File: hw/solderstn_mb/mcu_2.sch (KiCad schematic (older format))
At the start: 21 parts, among them U401 STM32F429VITx, U402 REF6125IDGK, U403 TLV9052SIDGS

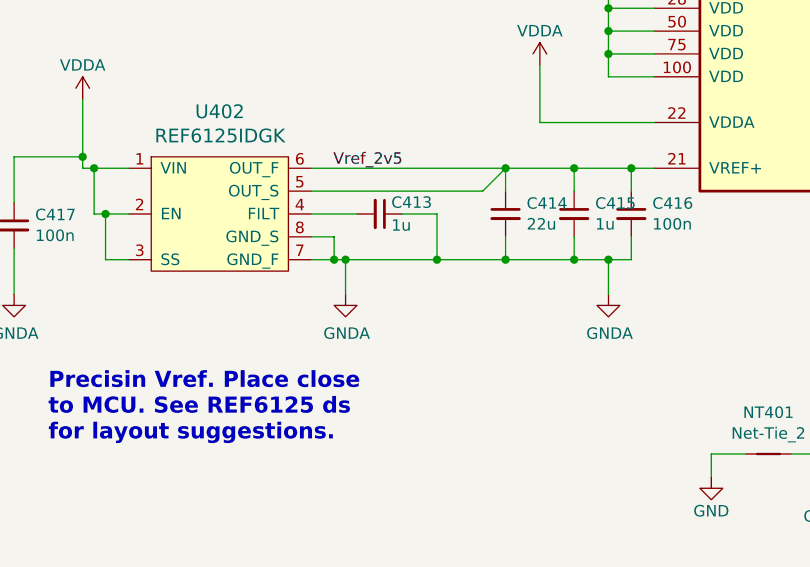
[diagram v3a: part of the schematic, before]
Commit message: Corrected several ERC issues. Re-annotated & assigned all footprints except 32k xtal (will prob. replace with RTC module anyway)
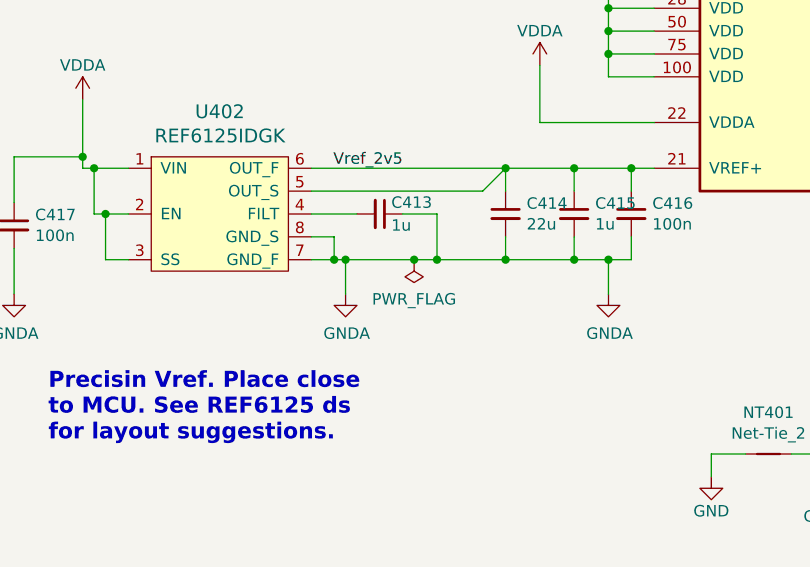
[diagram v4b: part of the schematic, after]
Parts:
- C401, C409, C410, C411, C412, C413, C414, C415, C416, C417: footprint (none) -> Capacitor_SMD:C_0603_1608Metric
- C402, C403, C404, C405, C406, C407, C408: footprint (none) -> Capacitor_SMD:C_0402_1005Metric
- NT401: footprint (none) -> NetTie:NetTie-2_SMD_Pad2.0mm
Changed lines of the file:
@@
 F 0 "C414" H 4442 3546 50  0000 L CNN
 F 1 "22u" H 4442 3455 50  0000 L CNN
-F 2 "" H 4350 3500 50  0001 C CNN
+F 2 "Capacitor_SMD:C_0603_1608Metric" H 4350 3500 50  0001 C CNN
 F 3 "~" H 4350 3500 50  0001 C CNN
 	1    4350 3500
@@
 F 0 "C413" V 3750 3550 50  0000 L CNN
 F 1 "1u" V 3850 3550 50  0000 L CNN
-F 2 "" H 3800 3500 50  0001 C CNN
+F 2 "Capacitor_SMD:C_0603_1608Metric" H 3800 3500 50  0001 C CNN
 F 3 "~" H 3800 3500 50  0001 C CNN
 	1    3800 3500
@@
 Connection ~ 4050 3700
 Wire Wire Line
-	4050 3700 3650 3700
+	4050 3700 3950 3700
 Wire Wire Line
 	3700 3500 3500 3500
@@
 F 0 "C417" H 2292 3596 50  0000 L CNN
 F 1 "100n" H 2292 3505 50  0000 L CNN
-F 2 "" H 2200 3550 50  0001 C CNN
+F 2 "Capacitor_SMD:C_0603_1608Metric" H 2200 3550 50  0001 C CNN
 F 3 "~" H 2200 3550 50  0001 C CNN
 	1    2200 3550
@@
 F 0 "C411" H 8242 3296 50  0000 L CNN
 F 1 "100n" H 8242 3205 50  0000 L CNN
-F 2 "" H 8150 3250 50  0001 C CNN
+F 2 "Capacitor_SMD:C_0603_1608Metric" H 8150 3250 50  0001 C CNN
 F 3 "~" H 8150 3250 50  0001 C CNN
 	1    8150 3250
@@
 F 0 "C408" H 10142 2296 50  0000 L CNN
 F 1 "100n" H 10142 2205 50  0000 L CNN
-F 2 "" H 10050 2250 50  0001 C CNN
+F 2 "Capacitor_SMD:C_0402_1005Metric" H 10050 2250 50  0001 C CNN
 F 3 "~" H 10050 2250 50  0001 C CNN
 	1    10050 2250
@@
 F 0 "C407" H 9792 2296 50  0000 L CNN
 F 1 "100n" H 9792 2205 50  0000 L CNN
-F 2 "" H 9700 2250 50  0001 C CNN
+F 2 "Capacitor_SMD:C_0402_1005Metric" H 9700 2250 50  0001 C CNN
 F 3 "~" H 9700 2250 50  0001 C CNN
 	1    9700 2250
@@
 F 0 "C406" H 9442 2296 50  0000 L CNN
 F 1 "100n" H 9442 2205 50  0000 L CNN
-F 2 "" H 9350 2250 50  0001 C CNN
+F 2 "Capacitor_SMD:C_0402_1005Metric" H 9350 2250 50  0001 C CNN
 F 3 "~" H 9350 2250 50  0001 C CNN
 	1    9350 2250
@@
 F 0 "C405" H 9092 2296 50  0000 L CNN
 F 1 "100n" H 9092 2205 50  0000 L CNN
-F 2 "" H 9000 2250 50  0001 C CNN
+F 2 "Capacitor_SMD:C_0402_1005Metric" H 9000 2250 50  0001 C CNN
 F 3 "~" H 9000 2250 50  0001 C CNN
 	1    9000 2250
@@
 F 0 "C404" H 8742 2296 50  0000 L CNN
 F 1 "100n" H 8742 2205 50  0000 L CNN
-F 2 "" H 8650 2250 50  0001 C CNN
+F 2 "Capacitor_SMD:C_0402_1005Metric" H 8650 2250 50  0001 C CNN
 F 3 "~" H 8650 2250 50  0001 C CNN
 	1    8650 2250
@@
 F 0 "C403" H 8392 2296 50  0000 L CNN
 F 1 "100n" H 8392 2205 50  0000 L CNN
-F 2 "" H 8300 2250 50  0001 C CNN
+F 2 "Capacitor_SMD:C_0402_1005Metric" H 8300 2250 50  0001 C CNN
 F 3 "~" H 8300 2250 50  0001 C CNN
 	1    8300 2250
@@
 F 0 "C402" H 8042 2296 50  0000 L CNN
 F 1 "100n" H 8042 2205 50  0000 L CNN
-F 2 "" H 7950 2250 50  0001 C CNN
+F 2 "Capacitor_SMD:C_0402_1005Metric" H 7950 2250 50  0001 C CNN
 F 3 "~" H 7950 2250 50  0001 C CNN
 	1    7950 2250
@@
 F 0 "C401" H 7692 2296 50  0000 L CNN
 F 1 "10u" H 7692 2205 50  0000 L CNN
-F 2 "" H 7600 2250 50  0001 C CNN
+F 2 "Capacitor_SMD:C_0603_1608Metric" H 7600 2250 50  0001 C CNN
 F 3 "~" H 7600 2250 50  0001 C CNN
 	1    7600 2250
@@
 F 0 "NT401" H 5500 4731 50  0000 C CNN
 F 1 "Net-Tie_2" H 5500 4640 50  0000 C CNN
-F 2 "" H 5500 4550 50  0001 C CNN
+F 2 "NetTie:NetTie-2_SMD_Pad2.0mm" H 5500 4550 50  0001 C CNN
 F 3 "~" H 5500 4550 50  0001 C CNN
 	1    5500 4550
@@
 F 0 "C412" H 8592 3296 50  0000 L CNN
 F 1 "1u" H 8592 3205 50  0000 L CNN
-F 2 "" H 8500 3250 50  0001 C CNN
+F 2 "Capacitor_SMD:C_0603_1608Metric" H 8500 3250 50  0001 C CNN
 F 3 "~" H 8500 3250 50  0001 C CNN
 	1    8500 3250
@@
 F 0 "C415" H 4742 3546 50  0000 L CNN
 F 1 "1u" H 4742 3455 50  0000 L CNN
-F 2 "" H 4650 3500 50  0001 C CNN
+F 2 "Capacitor_SMD:C_0603_1608Metric" H 4650 3500 50  0001 C CNN
 F 3 "~" H 4650 3500 50  0001 C CNN
 	1    4650 3500
@@
 F 0 "C416" H 4992 3546 50  0000 L CNN
 F 1 "100n" H 4992 3455 50  0000 L CNN
-F 2 "" H 4900 3500 50  0001 C CNN
+F 2 "Capacitor_SMD:C_0603_1608Metric" H 4900 3500 50  0001 C CNN
 F 3 "~" H 4900 3500 50  0001 C CNN
 	1    4900 3500
@@
 F 0 "C409" H 6442 2596 50  0000 L CNN
 F 1 "2u2" H 6442 2505 50  0000 L CNN
-F 2 "" H 6350 2550 50  0001 C CNN
+F 2 "Capacitor_SMD:C_0603_1608Metric" H 6350 2550 50  0001 C CNN
 F 3 "~" H 6350 2550 50  0001 C CNN
 	1    6350 2550
@@
 F 0 "C410" H 6792 2596 50  0000 L CNN
 F 1 "2u2" H 6792 2505 50  0000 L CNN
-F 2 "" H 6700 2550 50  0001 C CNN
+F 2 "Capacitor_SMD:C_0603_1608Metric" H 6700 2550 50  0001 C CNN
 F 3 "~" H 6700 2550 50  0001 C CNN
 	1    6700 2550
@@
 Wire Wire Line
 	6000 5500 6000 5700
+$Comp
+L power:PWR_FLAG #FLG0401
+U 1 1 5F4FFBF9
+P 3950 3700
+F 0 "#FLG0401" H 3950 3775 50  0001 C CNN
+F 1 "PWR_FLAG" H 3950 3873 50  0000 C CNN
+F 2 "" H 3950 3700 50  0001 C CNN
+F 3 "~" H 3950 3700 50  0001 C CNN
+	1    3950 3700
+	-1   0    0    1
+$EndComp
+Connection ~ 3950 3700
+Wire Wire Line
+	3950 3700 3650 3700
 $EndSCHEMATC

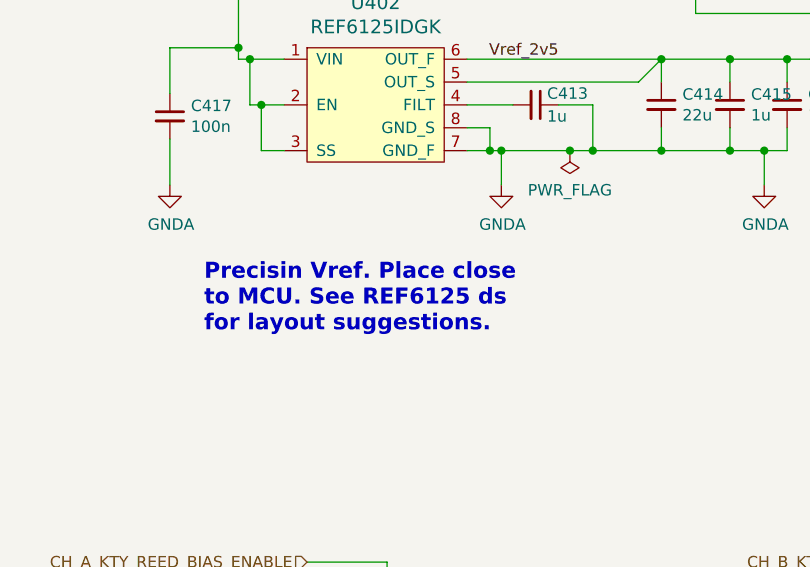
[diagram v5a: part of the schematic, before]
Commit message: MB: *) add LED on DC-in pwr-rail *) fix misnamed audio signals
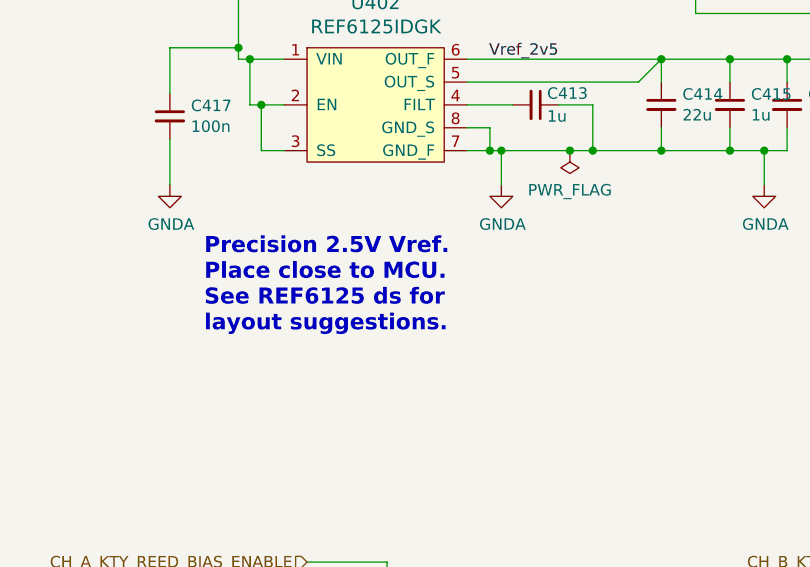
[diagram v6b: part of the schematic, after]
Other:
- note added: "Precision 2.5V Vref.\nPlace close to MCU.\nSee REF6125 ds for\nlayout suggestions."
- note removed: "Precisin Vref. Place close\nto MCU. See REF6125 ds\nfor layout suggestions."
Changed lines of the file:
@@
 MCU decoupling - place close to MCU power pins
 Text Notes 2350 4500 0    70   ~ 14
-Precisin Vref. Place close\nto MCU. See REF6125 ds\nfor layout suggestions.
+Precision 2.5V Vref.\nPlace close to MCU.\nSee REF6125 ds for\nlayout suggestions.
 Text Notes 3050 7050 0    70   ~ 14
 Switchable Vref for biasing KTY sensors\n(for cold-junction compensation), one\nper channel. The KTY's can then be\nmeassured through the ordinary TC \namps.\n
